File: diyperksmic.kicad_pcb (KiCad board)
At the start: 2 copper layers, 125 x 70 mm, 25 parts, among them J1 Conn_01x03, J2 Conn_Coaxial, J3 Conn_01x02, J4 Conn_01x02, U1 THAT1512, U2 NMA0515SC

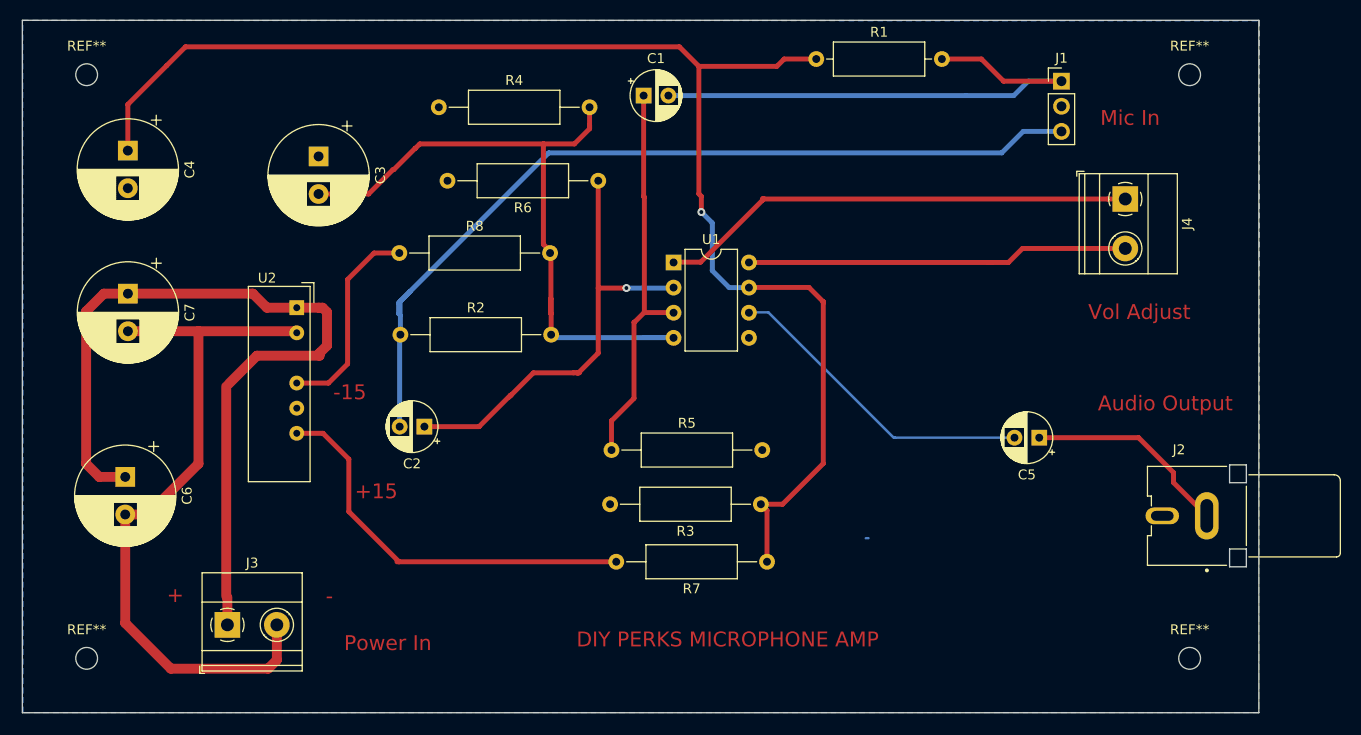
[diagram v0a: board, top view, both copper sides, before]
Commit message: updated kicad board
fix resistor sizes and cap sizes
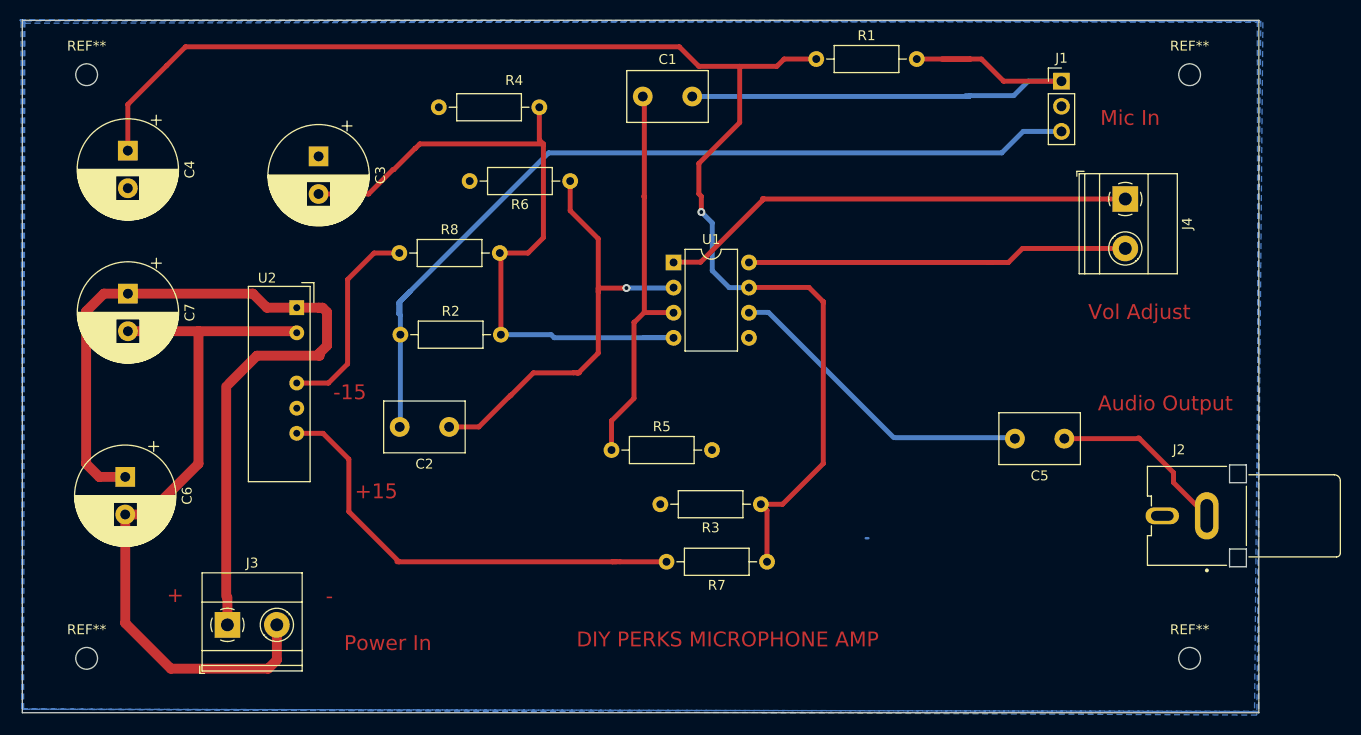
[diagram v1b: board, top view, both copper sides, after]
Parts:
- C1, C2, C5: footprint Capacitor_THT:CP_Radial_D5.0mm_P2.50mm -> Capacitor_THT:C_Disc_D8.0mm_W5.0mm_P5.00mm
- R1: footprint Resistor_THT:R_Axial_DIN0309_L9.0mm_D3.2mm_P12.70mm_Horizontal -> Resistor_THT:R_Axial_DIN0207_L6.3mm_D2.5mm_P10.16mm_Horizontal
- R2, R3, R4, R5, R6, R7, R8: footprint Resistor_THT:R_Axial_DIN0309_L9.0mm_D3.2mm_P15.24mm_Horizontal -> Resistor_THT:R_Axial_DIN0207_L6.3mm_D2.5mm_P10.16mm_Horizontal
- moved R6 2.84 mm to (133.4, 56.3)
- moved C5 2.54 mm to (183.3, 82.3)
- moved C2 2.50 mm to (121.1, 81.1)
- moved C1 0.13 mm to (140.7, 47.7)
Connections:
- U1 pad 5: GND -> Net-(U1-Pad5)
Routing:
- net Net-(R7-Pad2): track 41.0 -> 46.5 mm
- net Net-(C1-Pad2): track 53.4 -> 56.9 mm
- net -15V: track 69.1 -> 72.0 mm
- net Net-(C5-Pad1): track 20.8 -> 18.4 mm
- net +15V: track 142.1 -> 143.8 mm
- net Net-(C2-Pad1): track 46.2 -> 45.3 mm
